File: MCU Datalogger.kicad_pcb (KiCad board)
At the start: 2 copper layers, 47.6 x 30.5 mm, 29 parts, among them J1 Conn_01x04_Pin, J2 Conn_01x04_Pin, J3 Conn_01x09_Pin, J4 Conn_02x03_Odd_Even, U1 24LC1025, U2 24LC1025, U3 DS1337S_, U4 ATMEGA328P-AU, Y1 32.768 KHz, Y2 16 MHz

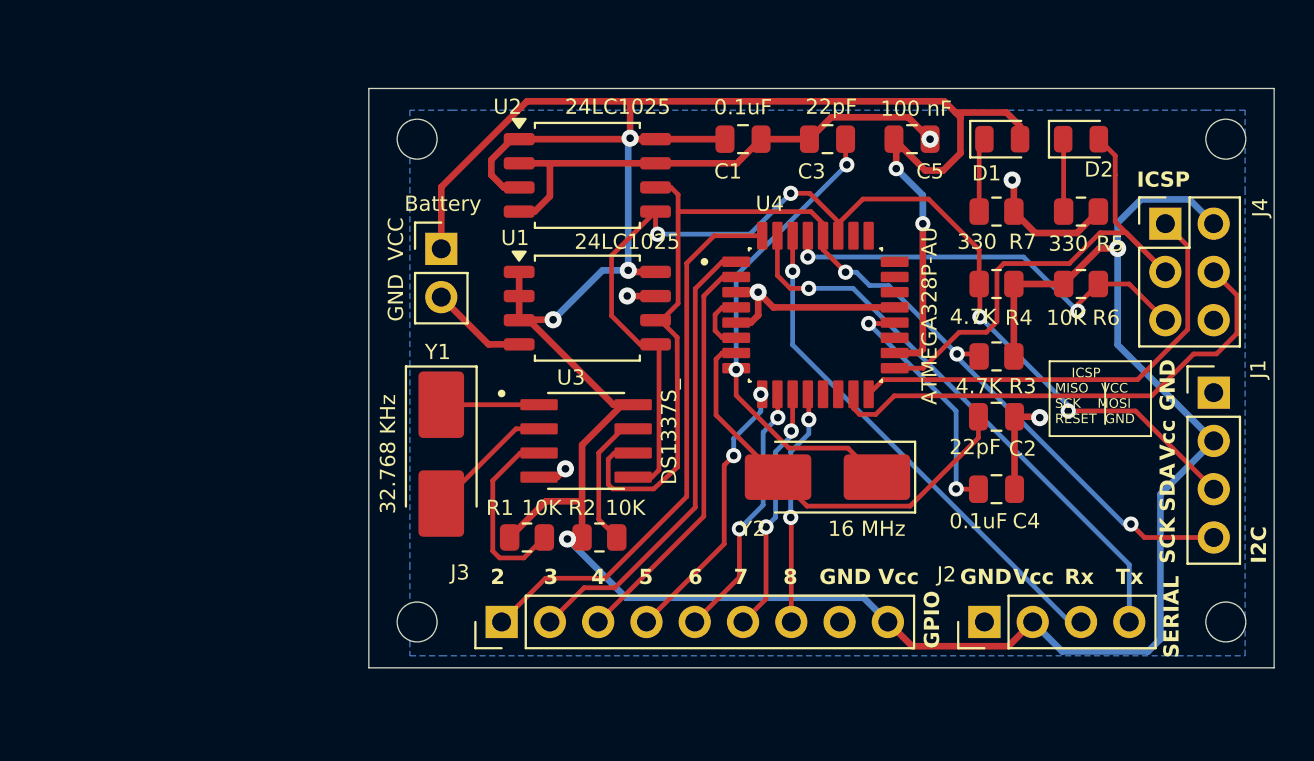
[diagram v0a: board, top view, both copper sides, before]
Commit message: completed 4 layer layout.
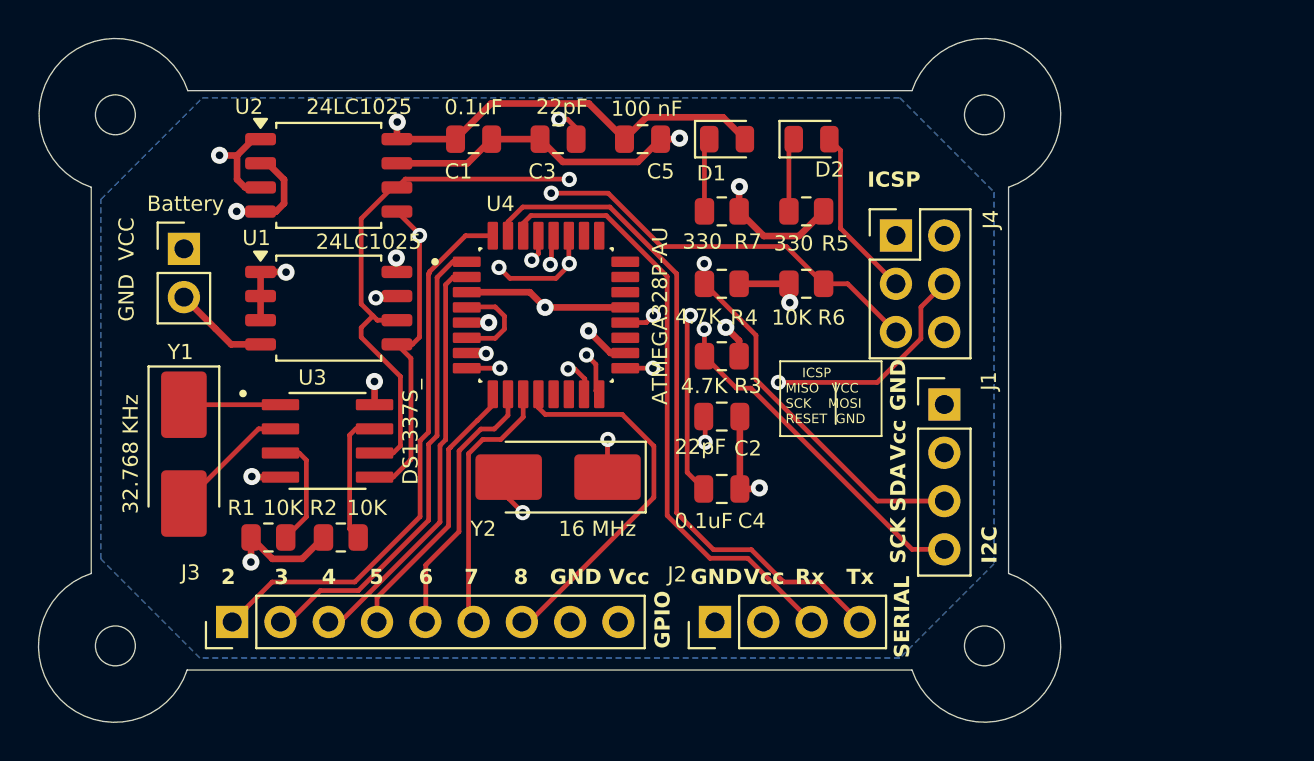
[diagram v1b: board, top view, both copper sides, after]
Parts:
- moved H1 15.9 mm to (52.1, 90.2)
- moved H2 15.9 mm to (52.1, 118.1)
- moved D1 14.5 mm to (84.2, 91.5)
- moved C2 14.5 mm to (84.0, 106.0)
- moved C4 14.5 mm to (84.0, 109.9)
- moved R3 14.5 mm to (84.0, 102.9)
- moved R4 14.5 mm to (84.0, 99.1)
- moved R5 14.5 mm to (88.4, 95.2)
- moved R6 14.5 mm to (88.4, 99.1)
- moved R7 14.5 mm to (84.0, 95.2)
- moved J1 14.2 mm to (95.7, 105.4)
- moved J4 14.2 mm to (93.1, 96.5)
- moved D2 14.2 mm to (88.7, 91.5)
- moved J2 14.2 mm to (83.6, 116.9)
- moved U4 14.2 mm to (74.7, 100.7)
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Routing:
- net /Vcc: track 189.9 -> 46.8 mm, vias 7 -> 9
- net GND: track 59.6 -> 51.2 mm, vias 6 -> 8
- net /D8: track 12.4 -> 20.0 mm, vias 2 -> 0
- net /TX: track 29.9 -> 36.0 mm, vias 1 -> 0
- net /SDA: track 60.0 -> 54.6 mm
- net /RX: track 27.0 -> 32.2 mm, vias 1 -> 0
- net Net-(U3-~{INTA}): track 10.1 -> 6.03 mm
- net /RESET: track 22.7 -> 26.5 mm
- net /MISO: track 24.3 -> 21.2 mm, vias 0 -> 1
- net /SCK: track 28.1 -> 25.1 mm, vias 0 -> 1
- net Net-(U4-PB6): track 22.5 -> 25.3 mm, vias 0 -> 3
- net Net-(U4-PB7): track 25.2 -> 27.0 mm, vias 2 -> 3
- net VCC: track 3.38 -> 5.07 mm
- net /MOSI: track 26.6 -> 25.1 mm, vias 0 -> 2
- net /SCL: track 61.3 -> 62.4 mm
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- added copper zone on In2.Cu, net /Vcc
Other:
- board size 47.6 x 30.5 mm -> 53.8 x 36 mm
- copper layers 2 -> 4
- board text added: "53.7865 mm x 35.9811 mm"
- board text removed: "47.6250 mm x 30.4800 mm"
